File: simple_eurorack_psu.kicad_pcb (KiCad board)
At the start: 2 copper layers, 135 x 75 mm, 36 parts, among them J1 AC_IN_1, J2 AC_IN_2, J3 POWER_OUT_0, J4 POWER_OUT_1, J5 POWER_OUT_2, J6 POWER_OUT_3, U1 NJM7812, U2 NJM7912, U3 NJM7805

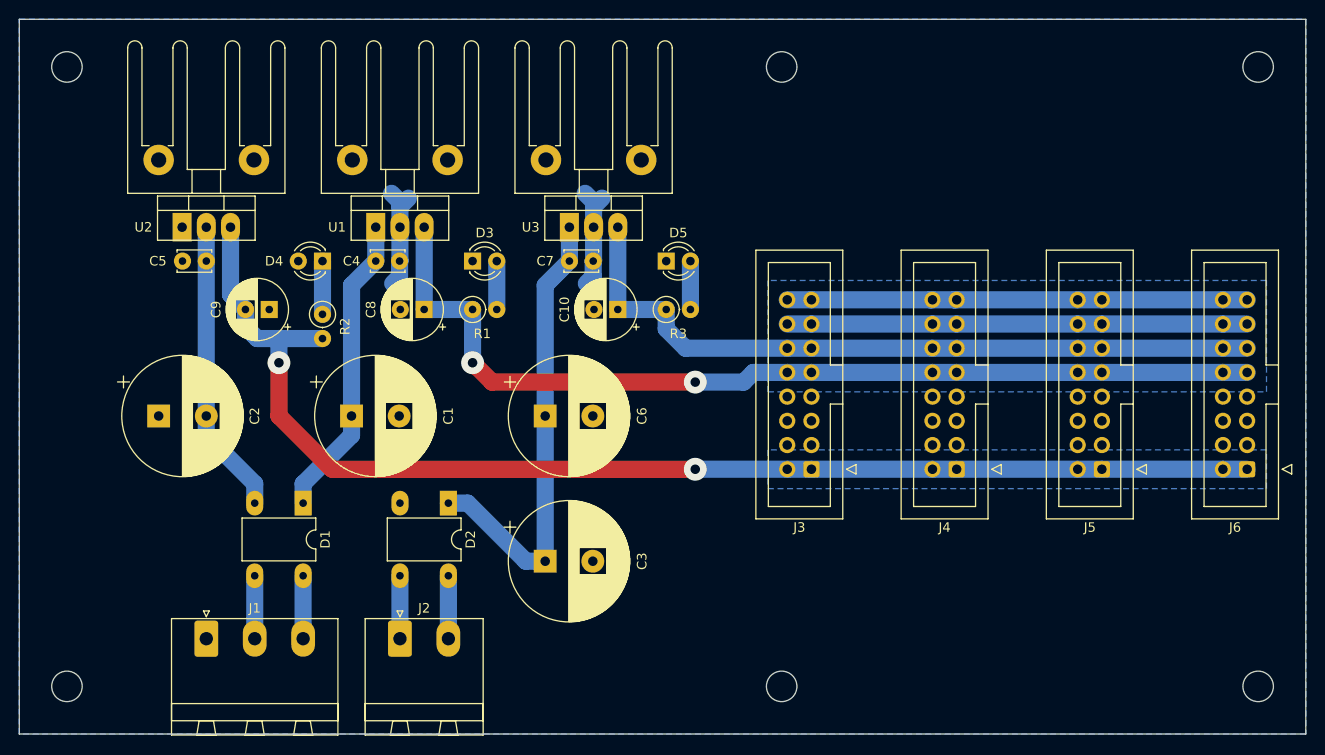
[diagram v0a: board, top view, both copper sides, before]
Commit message: reposition capacitors
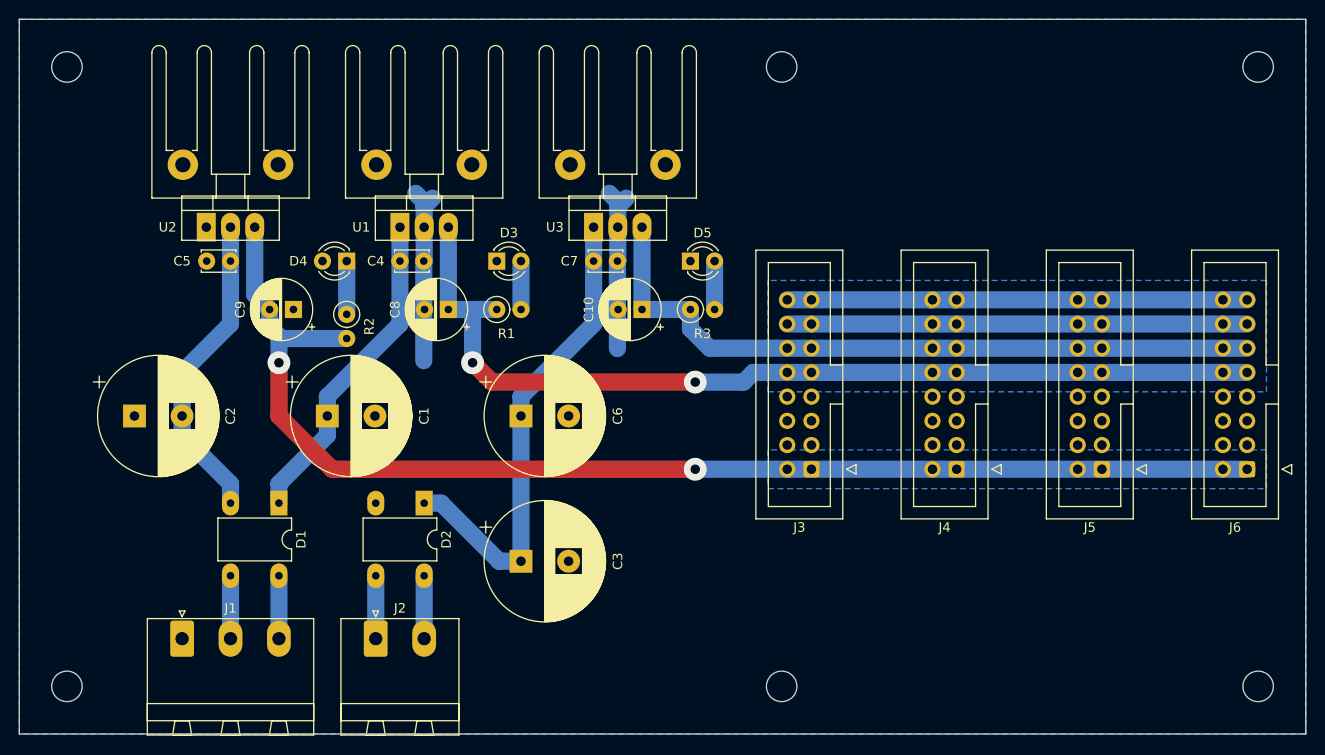
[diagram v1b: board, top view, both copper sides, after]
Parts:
- moved HS3 2.59 mm to (82.8, 48.8)
- moved HS1 2.59 mm to (62.5, 48.8)
- moved HS2 2.59 mm to (42.2, 48.8)
- moved D3 2.54 mm to (70.1, 55.4)
- moved D5 2.54 mm to (90.4, 55.4)
- moved R1 2.54 mm to (70.1, 60.5)
- moved R3 2.54 mm to (90.4, 60.5)
- moved C1 2.54 mm to (52.3, 71.6)
- moved C2 2.54 mm to (32.1, 71.6)
- moved C4 2.54 mm to (59.9, 55.4)
- moved C5 2.54 mm to (39.7, 55.4)
- moved C8 2.54 mm to (65.0, 60.5)
- moved C9 2.54 mm to (48.8, 60.5)
- moved D1 2.54 mm to (47.2, 80.8)
- moved D2 2.54 mm to (62.5, 80.8)
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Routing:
- net GND: track 22.9 -> 37.3 mm
- net +5V: track 77.5 -> 75.0 mm
- net /7912_VI: track 31.1 -> 33.2 mm
- net /7812_VI: track 32.1 -> 34.2 mm
- net /7805_VI: track 48.8 -> 50.9 mm
